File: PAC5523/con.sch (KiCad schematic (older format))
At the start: 37 parts, among them J10 NTC, J11 LED, J4 GND, J5 VIN, J6 UART, J7 ENCODER, J8 HALL, J9 AIN, P1 TC2030-CTX-Tag-Connect, Q2 Q_NMOS_GSD

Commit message: finalized board, silkscreen needs some work
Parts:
- added C42: 100p, Capacitor_SMD:C_0603_1608Metric, symbol Device:C_Small
- added R17: 4k3, Resistor_SMD:R_0603_1608Metric, symbol Device:R_Small
- added R6: 100k, Resistor_SMD:R_0603_1608Metric, symbol Device:R_Small
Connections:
- net GND: now also C42.2, R17.2
- net VIN: now also R6.1
- new net Vin_mon: C42.1, R17.1, R6.2
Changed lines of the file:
@@
 Text GLabel 6250 4300 3    50   Input ~ 0
 VIO
+$Comp
+L Device:R_Small R?
+U 1 1 5CEAA519
+P 7350 1450
+AR Path="/5CEAA519" Ref="R?"  Part="1"
+AR Path="/5D59ABFE/5CEAA519" Ref="R6"  Part="1"
+F 0 "R6" H 7409 1496 50  0000 L CNN
+F 1 "100k" H 7409 1405 50  0000 L CNN
+F 2 "Resistor_SMD:R_0603_1608Metric" H 7350 1450 50  0001 C CNN
+F 3 "~" H 7350 1450 50  0001 C CNN
+	1    7350 1450
+	1    0    0    -1
+$EndComp
+$Comp
+L Device:R_Small R?
+U 1 1 5CEAA51F
+P 7350 1750
+AR Path="/5CEAA51F" Ref="R?"  Part="1"
+AR Path="/5D59ABFE/5CEAA51F" Ref="R17"  Part="1"
+F 0 "R17" H 7409 1796 50  0000 L CNN
+F 1 "4k3" H 7409 1705 50  0000 L CNN
+F 2 "Resistor_SMD:R_0603_1608Metric" H 7350 1750 50  0001 C CNN
+F 3 "~" H 7350 1750 50  0001 C CNN
+	1    7350 1750
+	1    0    0    -1
+$EndComp
+$Comp
+L Device:C_Small C?
+U 1 1 5CEAA525
+P 7050 1750
+AR Path="/5CEAA525" Ref="C?"  Part="1"
+AR Path="/5D59ABFE/5CEAA525" Ref="C42"  Part="1"
+F 0 "C42" H 7142 1796 50  0000 L CNN
+F 1 "100p" H 7142 1705 50  0000 L CNN
+F 2 "Capacitor_SMD:C_0603_1608Metric" H 7050 1750 50  0001 C CNN
+F 3 "~" H 7050 1750 50  0001 C CNN
+	1    7050 1750
+	1    0    0    -1
+$EndComp
+$Comp
+L power:GND #PWR?
+U 1 1 5CEAA52B
+P 7350 1850
+AR Path="/5CEAA52B" Ref="#PWR?"  Part="1"
+AR Path="/5D59ABFE/5CEAA52B" Ref="#PWR0191"  Part="1"
+F 0 "#PWR0191" H 7350 1600 50  0001 C CNN
+F 1 "GND" H 7355 1677 50  0000 C CNN
+F 2 "" H 7350 1850 50  0001 C CNN
+F 3 "" H 7350 1850 50  0001 C CNN
+	1    7350 1850
+	1    0    0    -1
+$EndComp
+$Comp
+L power:GND #PWR?
+U 1 1 5CEAA531
+P 7050 1850
+AR Path="/5CEAA531" Ref="#PWR?"  Part="1"
+AR Path="/5D59ABFE/5CEAA531" Ref="#PWR0192"  Part="1"
+F 0 "#PWR0192" H 7050 1600 50  0001 C CNN
+F 1 "GND" H 7055 1677 50  0000 C CNN
+F 2 "" H 7050 1850 50  0001 C CNN
+F 3 "" H 7050 1850 50  0001 C CNN
+	1    7050 1850
+	1    0    0    -1
+$EndComp
+Wire Wire Line
+	7350 1550 7350 1600
+Wire Wire Line
+	7350 1600 7050 1600
+Wire Wire Line
+	7050 1600 7050 1650
+Connection ~ 7350 1600
+Wire Wire Line
+	7350 1600 7350 1650
+Text GLabel 7050 1600 0    50   Input ~ 0
+Vin_mon
+Text GLabel 7350 1350 1    50   Input ~ 0
+VIN
 $EndSCHEMATC

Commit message: finalized silkscreen
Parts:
- JP2: footprint Jumper:SolderJumper-3_P1.3mm_Open_Pad1.0x1.5mm_NumberLabels -> Jumper:SolderJumper-3_P1.3mm_Open_RoundedPad1.0x1.5mm
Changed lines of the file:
@@
 F 0 "JP2" H 4950 3204 50  0000 C CNN
 F 1 "UART" H 4950 3113 50  0000 C CNN
-F 2 "Jumper:SolderJumper-3_P1.3mm_Open_Pad1.0x1.5mm_NumberLabels" H 4950 3000 50  0001 C CNN
+F 2 "Jumper:SolderJumper-3_P1.3mm_Open_RoundedPad1.0x1.5mm" H 4950 3000 50  0001 C CNN
 F 3 "~" H 4950 3000 50  0001 C CNN
 	1    4950 3000

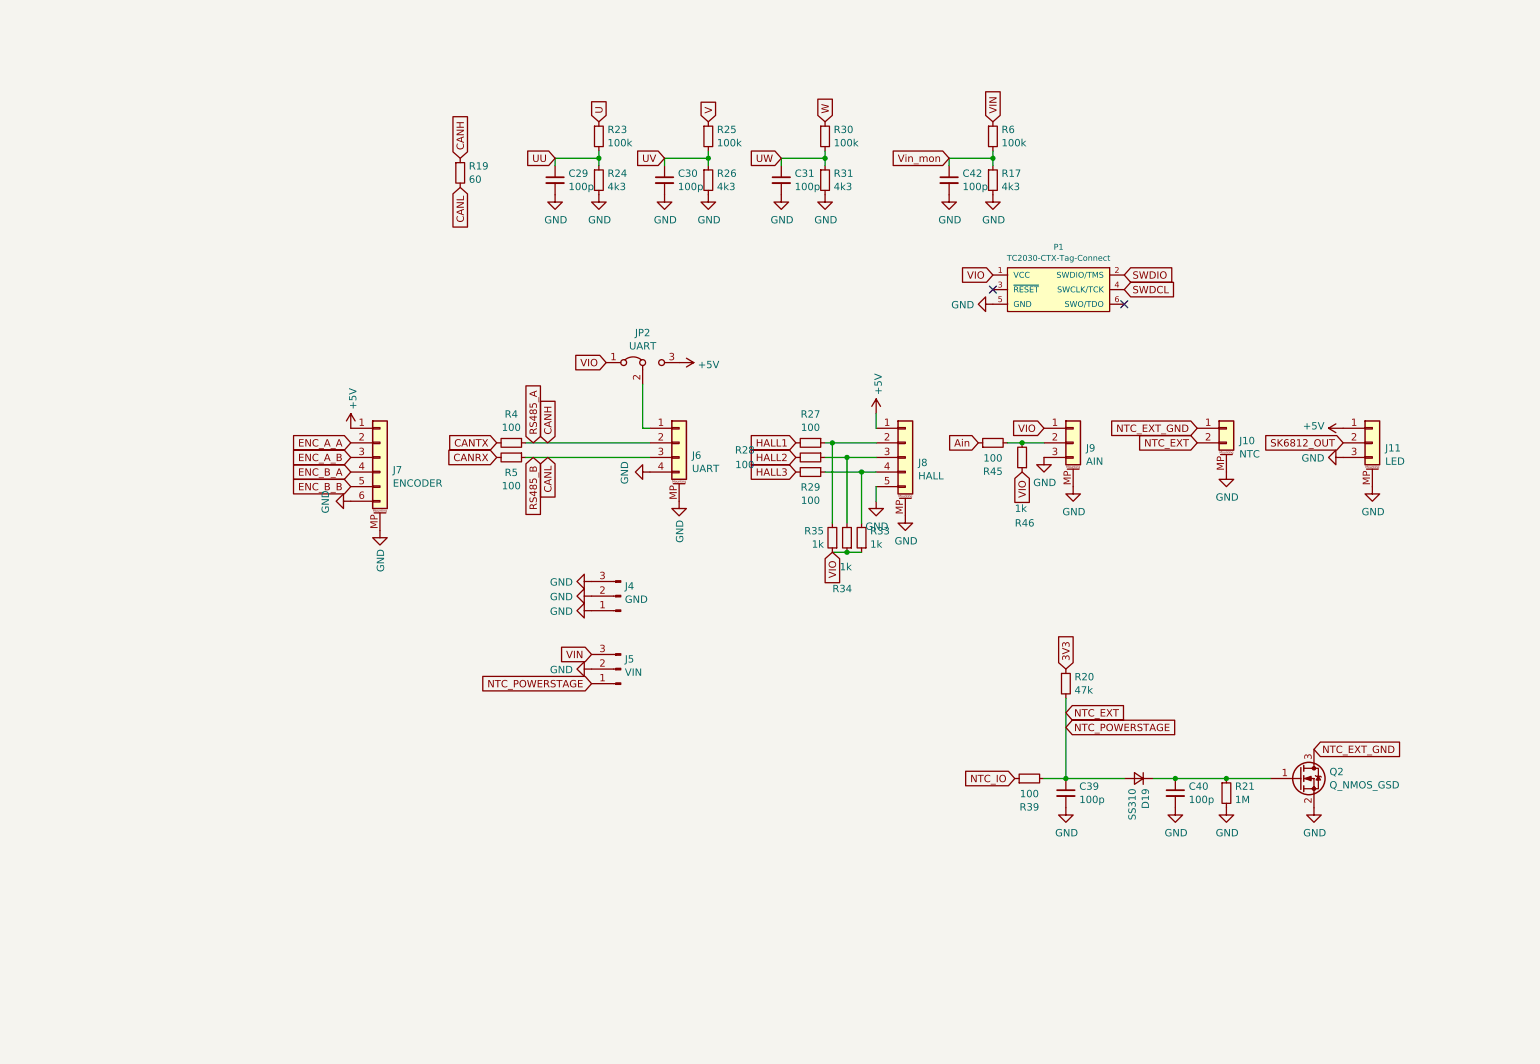
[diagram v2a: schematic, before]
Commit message: finalized silkscreen, generated gerber
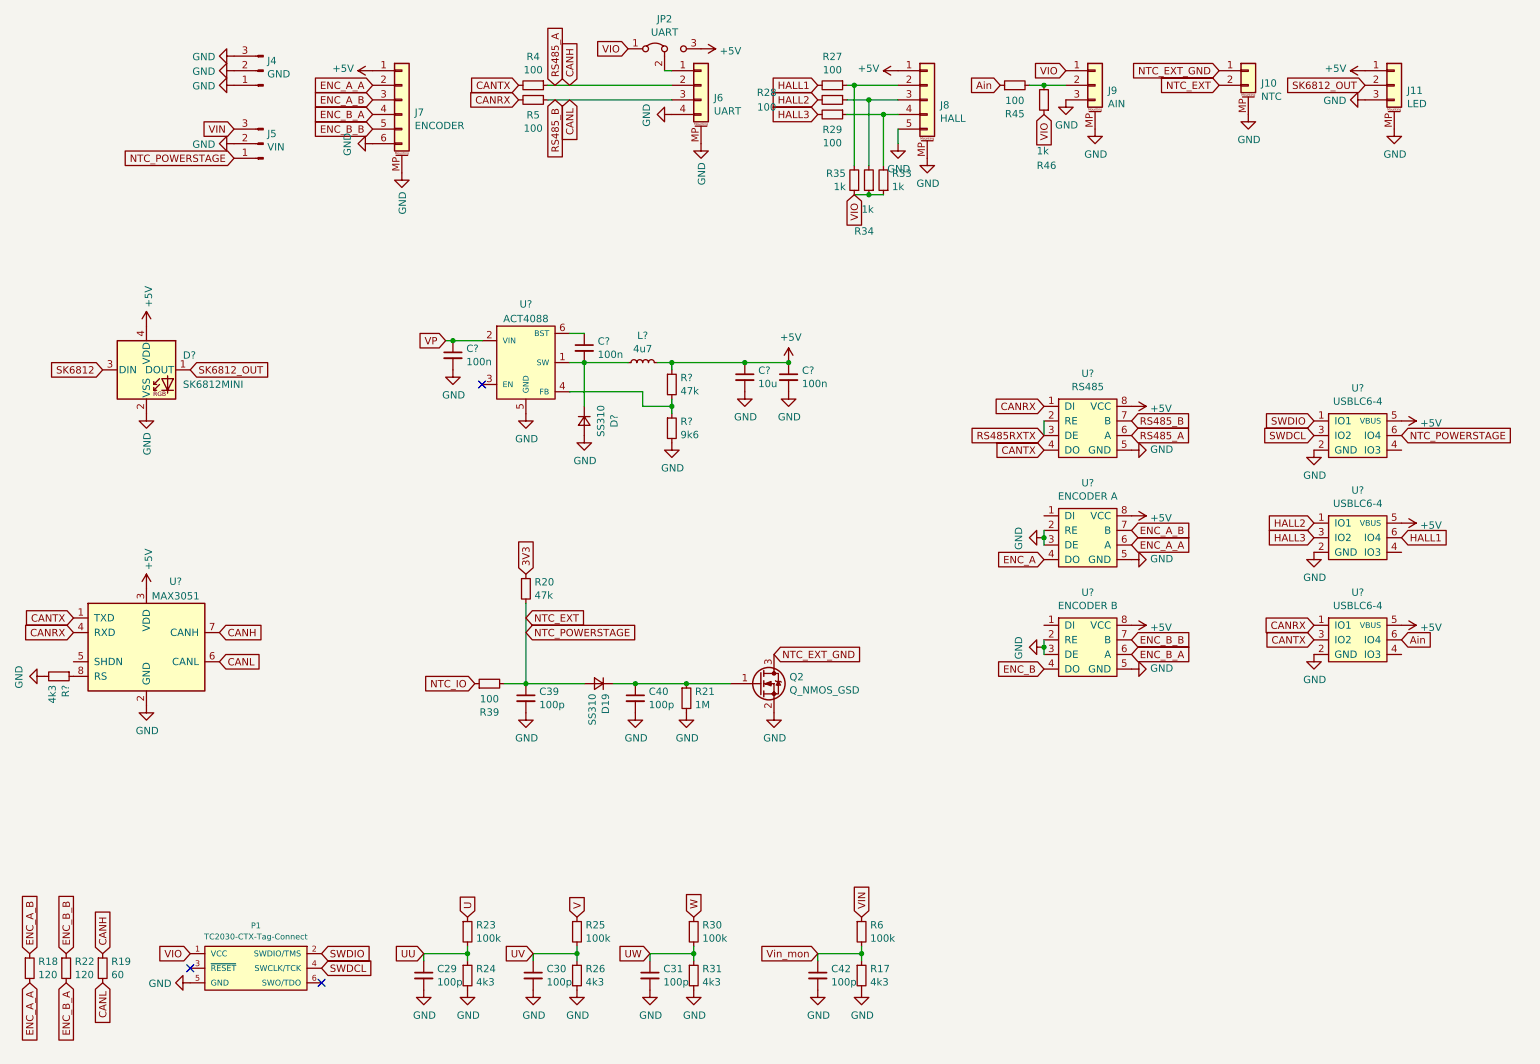
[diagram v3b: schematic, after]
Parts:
- added C? (x3): 100n, Capacitor_SMD:C_0603_1608Metric, symbol Device:C_Small
- added C?: 10u, Capacitor_SMD:C_1206_3216Metric, symbol Device:C_Small
- added D?: SS310, Diode_SMD:D_SOD-123F, symbol Device:D_Small
- added D?: SK6812MINI, LED_SMD:LED_SK6812MINI_PLCC4_3.5x3.5mm_P1.75mm, symbol LED:SK6812MINI
- added L?: 4u7, Inductor_SMD:L_Taiyo-Yuden_MD-4040, symbol Device:L_Small
- added R18, R22: 120, Resistor_SMD:R_0603_1608Metric, symbol Device:R_Small
- added R?: 9k6, Resistor_SMD:R_0603_1608Metric, symbol Device:R_Small
- added R?: 47k, Resistor_SMD:R_0603_1608Metric, symbol Device:R_Small
- added R?: 4k3, Resistor_SMD:R_0603_1608Metric, symbol Device:R_Small
- added U?: ACT4088, Package_TO_SOT_SMD:SOT-23-6, symbol otter:ACT4088
- added U?: MAX3051, Package_SO:SOIC-8_3.9x4.9mm_P1.27mm, symbol Interface_UART:MAX3051
- added U? (x3): USBLC6-4, Package_TO_SOT_SMD:SOT-23-6, symbol otter:USBLC6-4
- added U?: RS485, Package_SO:SOIC-8_3.9x4.9mm_P1.27mm, symbol otter:RS485
- added U?: ENCODER A, Package_SO:SOIC-8_3.9x4.9mm_P1.27mm, symbol otter:RS485
- added U?: ENCODER B, Package_SO:SOIC-8_3.9x4.9mm_P1.27mm, symbol otter:RS485
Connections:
- net +5V: now also C?.1, C?.1, D?.4 (VDD), L?.2, R?.1, U?.3 (VDD), U?.5 (VBUS), U?.5 (VBUS), U?.5 (VBUS), U?.8 (VCC), U?.8 (VCC), U?.8 (VCC)
- net Ain: now also U?.6 (IO4)
- net CANH: now also U?.6 (A), U?.7 (CANH)
- net CANL: now also U?.6 (CANL), U?.7 (B)
- net CANRX: now also U?.1 (DI), U?.1 (IO1), U?.4 (RXD)
- net CANTX: now also U?.1 (TXD), U?.3 (IO2), U?.4 (DO)
- net ENC_A_A: now also R18.2, U?.6 (A)
- net ENC_A_B: now also R18.1, U?.7 (B)
- net ENC_B_A: now also R22.2, U?.6 (A)
- net ENC_B_B: now also R22.1, U?.7 (B)
- net GND: now also C?.2, C?.2, C?.2, D?.2 (A), D?.2 (VSS), R?.2, R?.2, U?.2 (GND), U?.2 (GND), U?.2 (GND), U?.2 (GND), U?.2 (RE), U?.2 (RE), U?.3 (DE), U?.3 (DE), U?.5 (GND), U?.5 (GND), U?.5 (GND), U?.5 (GND)
- net HALL1: now also U?.6 (IO4)
- net HALL2: now also U?.1 (IO1)
- net HALL3: now also U?.3 (IO2)
- net NTC_EXT: now also U?.6 (IO4)
- net SK6812_OUT: now also D?.1 (DOUT)
- net SWDCL: now also U?.3 (IO2)
- net SWDIO: now also U?.1 (IO1)
- new net: R?.1, R?.2, U?.4 (FB)
- new net: C?.2, D?.1 (K), L?.1, U?.1 (SW)
- new net: C?.1, U?.6 (BST)
- new net: R?.1, U?.8 (RS)
- new net ENC_A: U?.4 (DO)
- new net ENC_B: U?.4 (DO)
- new net RS485RXTX: U?.2 (RE), U?.3 (DE)
- new net SK6812: D?.3 (DIN)
- new net VP: C?.1, U?.2 (VIN)
- no-connect marks 2 -> 3
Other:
- moved on the sheet: C29, C30, C31, C39, C40, C42, D19, J10, J11, J4, J5, J6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

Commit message: added gerber
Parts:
- R38: renamed from R?; value 9k6 -> 9k1
- gave numbers to parts that had none: 17
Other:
- note added: "CAP kleiner?"
